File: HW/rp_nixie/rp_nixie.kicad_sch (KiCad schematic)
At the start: 0 parts

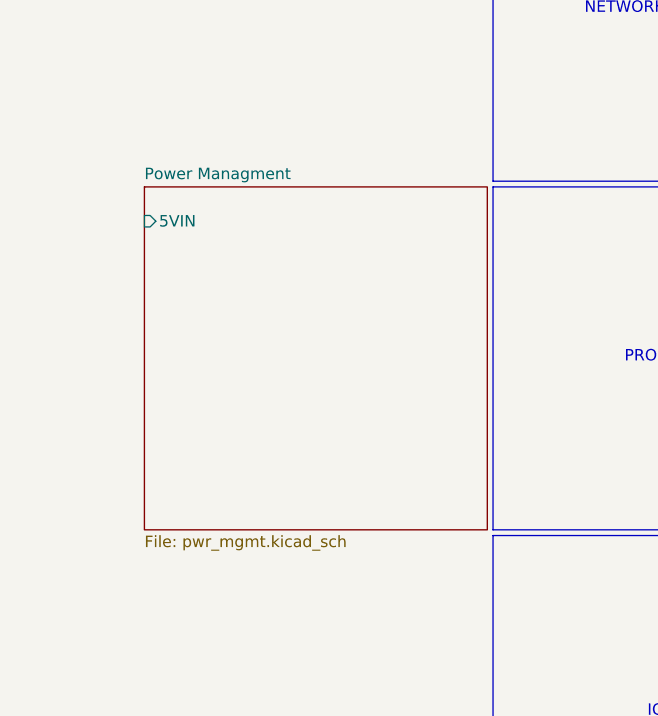
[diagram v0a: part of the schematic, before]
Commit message: added better boost circuit
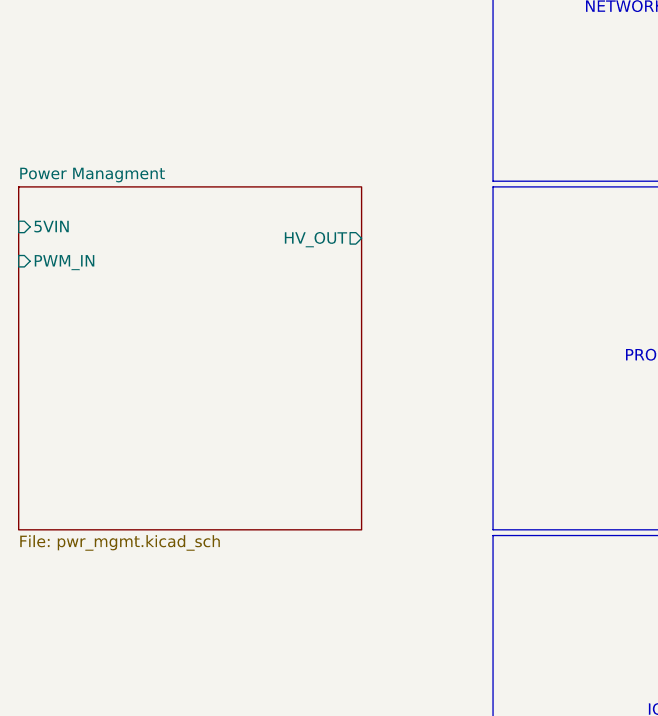
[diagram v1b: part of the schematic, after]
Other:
- sheet Power Managment ports: added HV_OUT, PWM_IN; removed none
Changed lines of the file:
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@@
     (effects (font (size 1.27 1.27)) (justify left bottom))
   )
-  (sheet (at 61.595 75.565) (size 38.1 38.1) (fields_autoplaced)
+  (sheet (at 47.625 75.565) (size 38.1 38.1) (fields_autoplaced)
     (stroke (width 0.1524) (type solid))
     (fill (color 0 0 0 0.0000))
-    (property "Sheetname" "Power Managment" (at 61.595 74.8534 0)
+    (property "Sheetname" "Power Managment" (at 47.625 74.8534 0)
       (effects (font (size 1.27 1.27)) (justify left bottom))
     )
-    (property "Sheetfile" "pwr_mgmt.kicad_sch" (at 61.595 114.2496 0)
+    (property "Sheetfile" "pwr_mgmt.kicad_sch" (at 47.625 114.2496 0)
       (effects (font (size 1.27 1.27)) (justify left top))
     )
-    (pin "5VIN" input (at 61.595 79.375 180)
+    (pin "5VIN" input (at 47.625 80.01 180)
       (effects (font (size 1.27 1.27)) (justify left))
     )
+    (pin "PWM_IN" input (at 47.625 83.82 180)
+      (effects (font (size 1.27 1.27)) (justify left))
+    )
+    (pin "HV_OUT" output (at 85.725 81.28 0)
+      (effects (font (size 1.27 1.27)) (justify right))
+    )
     (instances

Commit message: finished MCU and IO
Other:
- added sheet Display (display.kicad_sch)
- added sheet InputOutput (io.kicad_sch)
- added sheet MCU (mcu.kicad_sch)
- sheet Power Managment ports: added none; removed 5VIN, PWM_IN
- note removed: "DISPLAY"
- note removed: "IO"
- note removed: "NETWORKING/RTC"
- note removed: "PROCESSOR"

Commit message: some schematic work
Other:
- added sheet Driver (driver.kicad_sch)
- note removed: "DRIVER"
